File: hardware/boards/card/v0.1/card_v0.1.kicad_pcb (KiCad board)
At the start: 6 copper layers, 67.6 x 25.4 mm, 19 parts, among them IC1 IS42S16160J-7BLI, IC2 IS42S16160J-7BLI, J1 SODIMM-200, U2 STM32H747XIHx

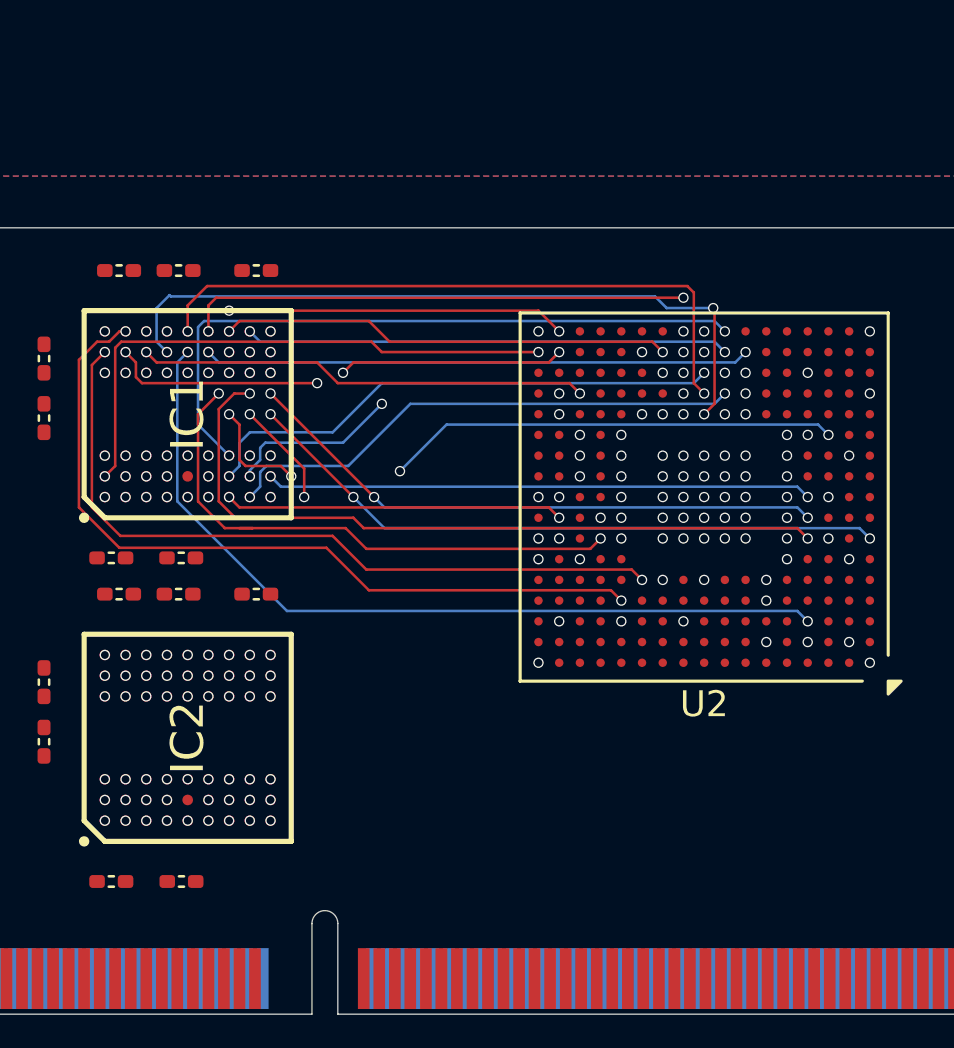
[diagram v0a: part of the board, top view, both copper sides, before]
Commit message: boards/card: begin routing USB differential pairs
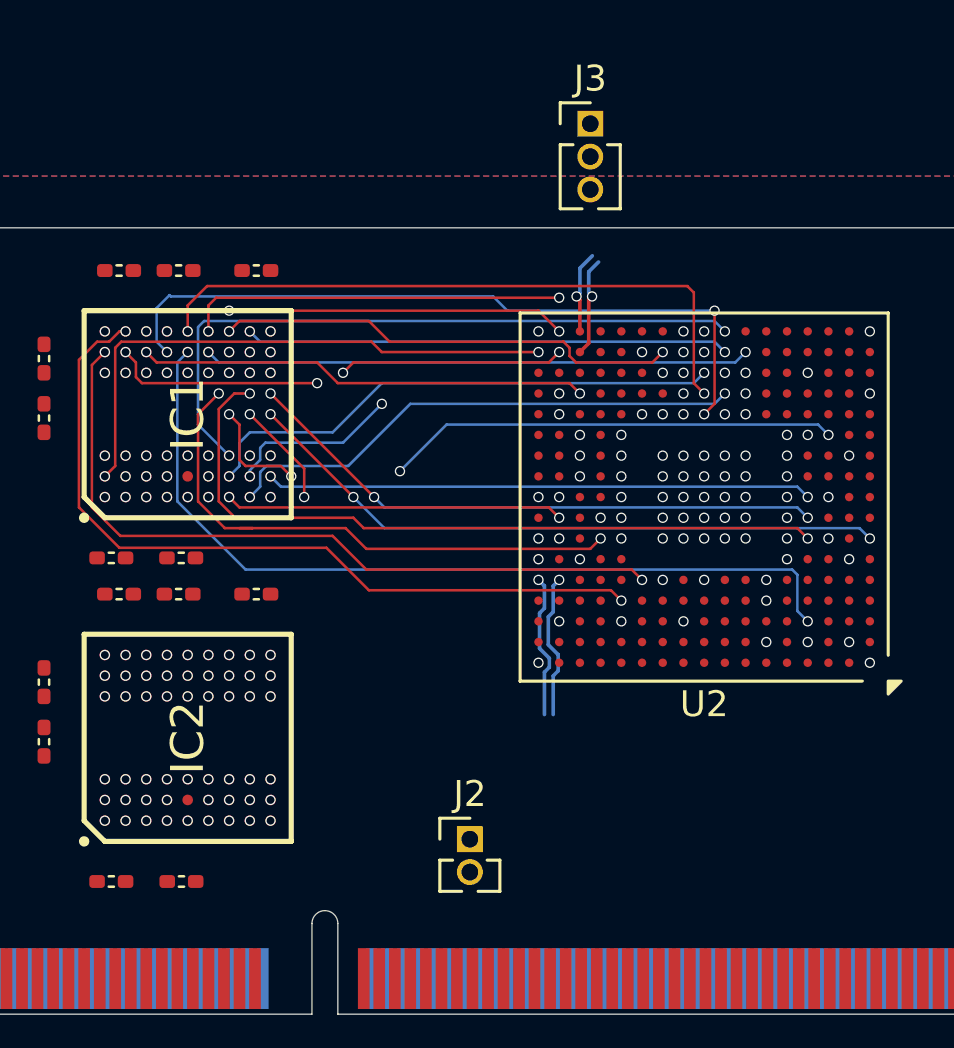
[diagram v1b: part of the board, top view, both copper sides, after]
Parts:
- added J2: USB_HOST, Connector_PinHeader_1.27mm:PinHeader_1x02_P1.27mm_Vertical, F.Cu at (71.7, 69.6)
- added J3: USB_DEVICE, Connector_PinHeader_1.27mm:PinHeader_1x03_P1.27mm_Vertical, F.Cu at (76.3, 42.0)
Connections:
- C10 pad 1: Net-(C10-Pad1) -> +3.3V
- C11 pad 1: Net-(C11-Pad1) -> +3.3V
- C12 pad 1: Net-(C11-Pad1) -> +3.3V
- C13 pad 1: Net-(C11-Pad1) -> +3.3V
- C14 pad 1: Net-(C11-Pad1) -> +3.3V
- C8 pad 1: Net-(C10-Pad1) -> +3.3V
- C9 pad 1: Net-(C10-Pad1) -> +3.3V
- IC2 pad A7: Net-(C11-Pad1) -> +3.3V
- IC2 pad A9: Net-(C10-Pad1) -> +3.3V
- IC2 pad B3: Net-(C11-Pad1) -> +3.3V
- IC2 pad C7: Net-(C11-Pad1) -> +3.3V
- IC2 pad D3: Net-(C11-Pad1) -> +3.3V
- IC2 pad E7: Net-(C10-Pad1) -> +3.3V
- IC2 pad J9: Net-(C10-Pad1) -> +3.3V
- U2 pad E16: unconnected-(U2-PA12-PadE16) -> /USB_OTG_FS_D+
- U2 pad E17: unconnected-(U2-PA11-PadE17) -> /USB_OTG_FS_D-
- U2 pad T15: unconnected-(U2-PB15-PadT15) -> /USB_OTG_HS_D+
- U2 pad U14: unconnected-(U2-PB13-PadU14) -> /USB_OTG_HS_VBUS
- U2 pad U15: unconnected-(U2-PB14-PadU15) -> /USB_OTG_HS_D-
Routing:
- net /USB_OTG_FS_D+: track 0.00 -> 5.61 mm, vias 0 -> 1
- net /USB_OTG_FS_D-: track 0.00 -> 5.61 mm, vias 0 -> 1
- net /USB_OTG_HS_D+: track 0.00 -> 3.89 mm, vias 0 -> 1
- net /USB_OTG_HS_D-: track 0.00 -> 3.23 mm, vias 0 -> 1
- net /FMC_NBL0: track 32.2 -> 33.0 mm
- net /FMC_SDNE1: track 17.4 -> 17.9 mm
- net Net-(C11-Pad1): vias 4 -> 0
- net Net-(C10-Pad1): vias 3 -> 0
- net +3.3V: vias 29 -> 36
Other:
- board text added: "Stackup: JLC06101H-3313 1mm thickness (inner 0.5Oz, outter 1Oz) USB: 90Ω Coplanar Differential Pair: 0.14mm width, 0.2mm spacing"

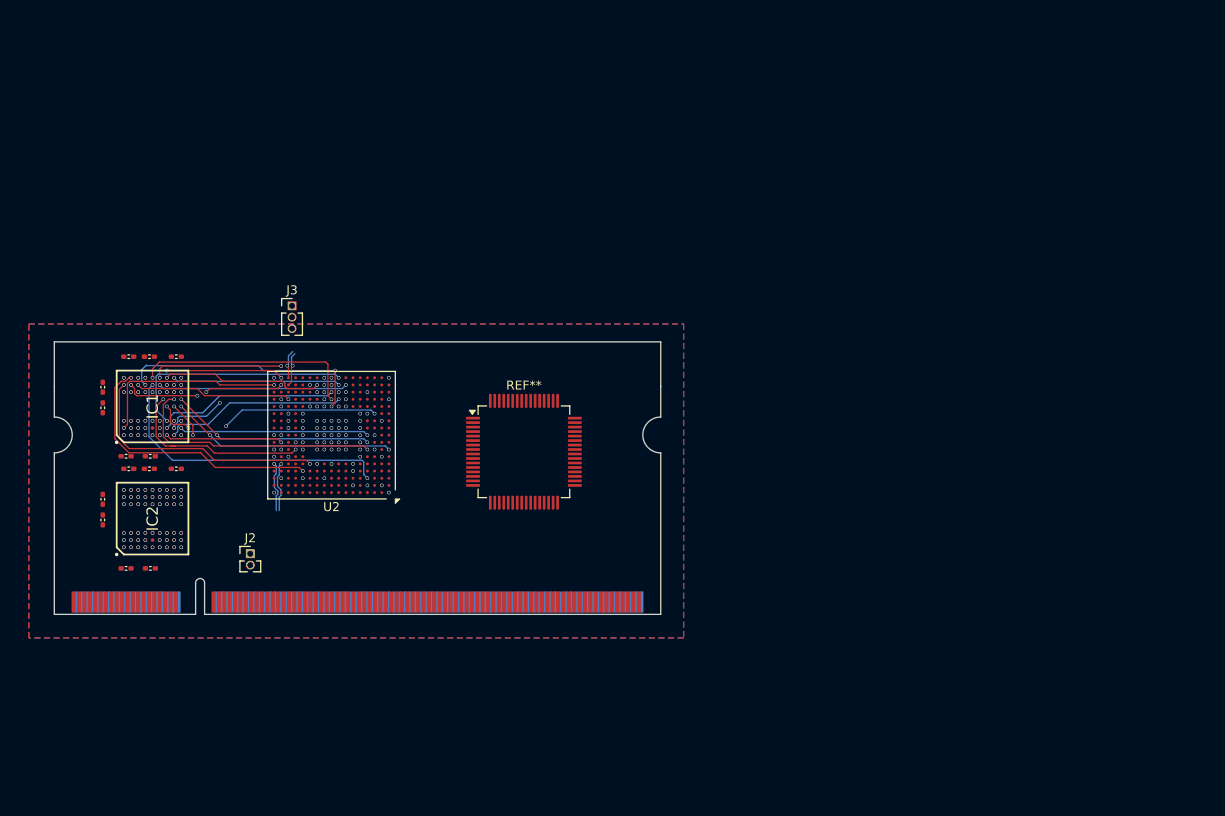
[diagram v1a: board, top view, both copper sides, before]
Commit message: boards/card: routing of essential components and audio codec
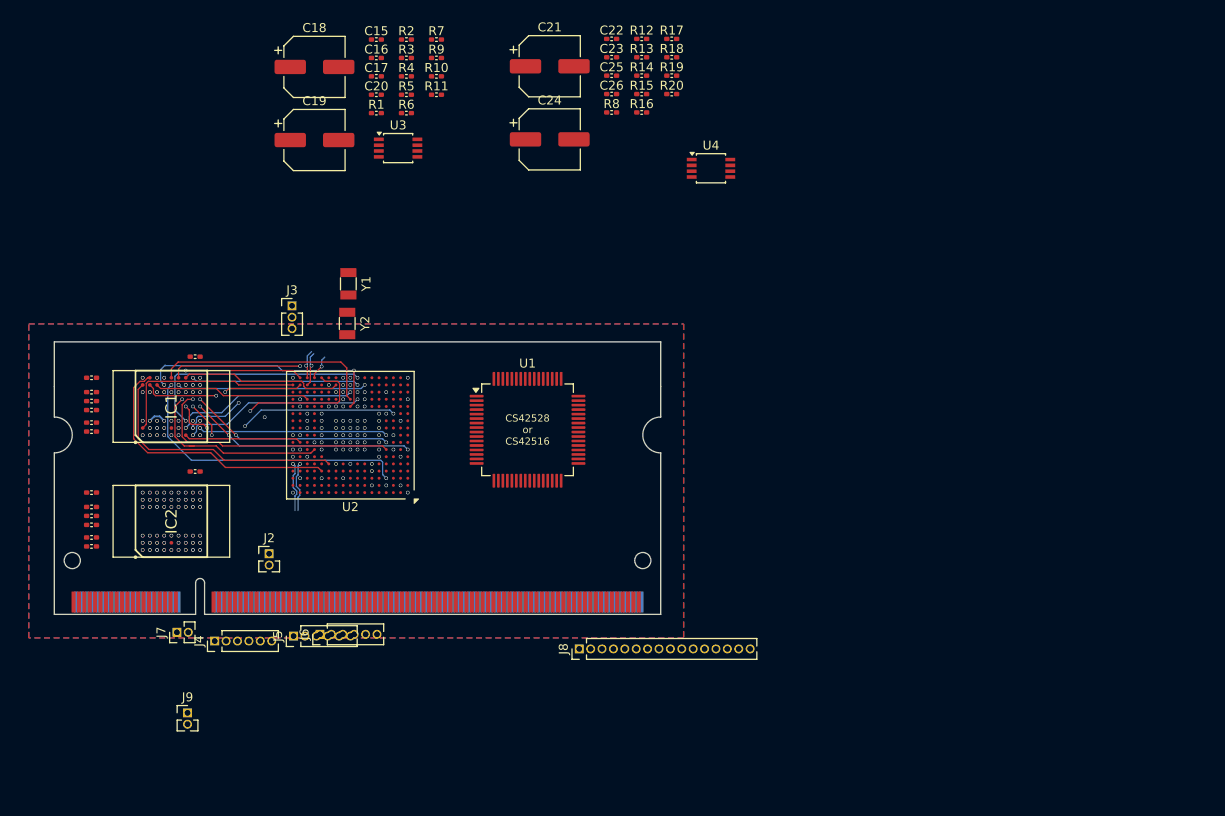
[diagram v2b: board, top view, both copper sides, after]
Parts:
- removed REF**: LQFP-64_10x10mm_P0.5mm, Package_QFP:LQFP-64_10x10mm_P0.5mm
- added C15: 2700pF C0G, rhais_rcl.pretty-main:C0402, F.Cu at (85.8, 12.3)
- added C16: 470pF C0G, rhais_rcl.pretty-main:C0402, F.Cu at (85.8, 14.3)
- added C17: 470pF C0G, rhais_rcl.pretty-main:C0402, F.Cu at (85.8, 16.4)
- added C18: 100uF ELEC, Capacitor_SMD:CP_Elec_6.3x5.7, F.Cu at (78.8, 15.3)
- added C19: 100uF ELEC, Capacitor_SMD:CP_Elec_6.3x5.7, F.Cu at (78.8, 23.5)
- added C20: 0.1uF X7R, rhais_rcl.pretty-main:C0402, F.Cu at (85.8, 18.4)
- added C21: 100uF ELEC, Capacitor_SMD:CP_Elec_6.3x5.7, F.Cu at (105.1, 15.3)
- added C22: 0.1uF X7R, rhais_rcl.pretty-main:C0402, F.Cu at (112.0, 12.2)
- added C23: 470pF C0G, rhais_rcl.pretty-main:C0402, F.Cu at (112.0, 14.3)
- added C24: 100uF ELEC, Capacitor_SMD:CP_Elec_6.3x5.7, F.Cu at (105.1, 23.4)
- added C25: 470pF C0G, rhais_rcl.pretty-main:C0402, F.Cu at (112.0, 16.3)
- added C26: 2700pF C0G, rhais_rcl.pretty-main:C0402, F.Cu at (112.0, 18.4)
- added J4: SD_CARD, Connector_PinHeader_1.27mm:PinHeader_1x06_P1.27mm_Vertical, F.Cu at (67.7, 79.3)
- added J5: DEBUG, Connector_PinHeader_1.27mm:PinHeader_1x06_P1.27mm_Vertical, F.Cu at (76.5, 78.8)
- added J6: SPI, Connector_PinHeader_1.27mm:PinHeader_1x06_P1.27mm_Vertical, F.Cu at (79.5, 78.6)
- added J7: UART4, Connector_PinHeader_1.27mm:PinHeader_1x02_P1.27mm_Vertical, F.Cu at (63.5, 78.4)
- added J8: Conn_01x16_Pin, Connector_PinHeader_1.27mm:PinHeader_1x16_P1.27mm_Vertical, F.Cu at (108.4, 80.2)
- added J9: AUDIO_IN, Connector_PinHeader_1.27mm:PinHeader_1x02_P1.27mm_Vertical, F.Cu at (64.7, 87.3)
- added R1: 91R, rhais_rcl.pretty-main:R0402, F.Cu at (85.8, 20.5)
- added R10: 3.32k, rhais_rcl.pretty-main:R0402, F.Cu at (92.5, 16.4)
- added R11: 100k, rhais_rcl.pretty-main:R0402, F.Cu at (92.5, 18.4)
- added R12: 100k, rhais_rcl.pretty-main:R0402, F.Cu at (115.3, 12.2)
- added R13: 2.8k, rhais_rcl.pretty-main:R0402, F.Cu at (115.3, 14.3)
- added R14: 3.32k, rhais_rcl.pretty-main:R0402, F.Cu at (115.3, 16.3)
- added R15: 634R, rhais_rcl.pretty-main:R0402, F.Cu at (115.3, 18.4)
- added R16: 332R, rhais_rcl.pretty-main:R0402, F.Cu at (115.3, 20.4)
- added R17: 634R, rhais_rcl.pretty-main:R0402, F.Cu at (118.7, 12.2)
- added R18: 91R, rhais_rcl.pretty-main:R0402, F.Cu at (118.7, 14.3)
- added R19: 634R, rhais_rcl.pretty-main:R0402, F.Cu at (118.7, 16.3)
- added R2: 634R, rhais_rcl.pretty-main:R0402, F.Cu at (89.1, 12.3)
- added R20: 91R, rhais_rcl.pretty-main:R0402, F.Cu at (118.7, 18.4)
- added R3: 634R, rhais_rcl.pretty-main:R0402, F.Cu at (89.1, 14.3)
- added R4: 91R, rhais_rcl.pretty-main:R0402, F.Cu at (89.1, 16.4)
- added R5: 634R, rhais_rcl.pretty-main:R0402, F.Cu at (89.1, 18.4)
- added R6: 332R, rhais_rcl.pretty-main:R0402, F.Cu at (89.1, 20.5)
- added R7: 10k, rhais_rcl.pretty-main:R0402, F.Cu at (92.5, 12.3)
- added R8: 10k, rhais_rcl.pretty-main:R0402, F.Cu at (112.0, 20.4)
- added R9: 2.8k, rhais_rcl.pretty-main:R0402, F.Cu at (92.5, 14.3)
- added U1: CS42528K-CQZ, Package_QFP:LQFP-64_10x10mm_P0.5mm, F.Cu at (102.6, 55.8)
- added U3: NJM4580E-TE1, Package_SO:TSSOP-8_3x3mm_P0.65mm, F.Cu at (88.2, 24.4)
- added U4: NJM4580E-TE1, Package_SO:TSSOP-8_3x3mm_P0.65mm, F.Cu at (123.0, 26.6)
- added Y1: Crystal, Crystal:Crystal_SMD_3215-2Pin_3.2x1.5mm, F.Cu at (82.6, 39.5)
- added Y2: Crystal, Crystal:Crystal_SMD_3215-2Pin_3.2x1.5mm, F.Cu at (82.5, 44.0)
- moved C9 8.98 mm to (54.0, 66.4)
- moved C2 7.56 mm to (54.0, 51.6)
- moved C6 7.10 mm to (54.0, 56.0), turned to 180 degrees
- moved C13 7.00 mm to (54.0, 68.8), turned to 180 degrees
- moved C5 5.37 mm to (54.0, 55.0)
- moved C14 5.17 mm to (54.0, 67.8)
- moved C10 4.92 mm to (54.0, 62.8), turned to 180 degrees
- moved C1 4.77 mm to (54.0, 50.0), turned to 180 degrees
- moved IC2 2.12 mm to (62.9, 66.0)
- moved C8 2.12 mm to (65.5, 60.5)
- moved IC1 2.10 mm to (62.9, 53.2)
- moved C3 2.10 mm to (65.5, 47.6)
- moved J2 2.10 mm to (73.8, 69.6)
- moved U2 2.10 mm to (82.8, 56.4)
- moved C4 1.99 mm to (54.0, 52.6), turned to 180 degrees
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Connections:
- IC1 pad F3: /FMC_SDCKE0 -> /FMC_SDCKE1
- IC2 pad F3: unconnected-(IC2-CKE-PadF3) -> /FMC_SDCKE0
- U2 pad A10: unconnected-(U2-PG9-PadA10) -> /SPI1_MISO
- U2 pad A13: unconnected-(U2-PC10-PadA13) -> /SDMMC1_D2
- U2 pad A2: unconnected-(U2-PI6-PadA2) -> /SAI2_SD_A
- U2 pad A9: unconnected-(U2-PG10-PadA9) -> /SPI1_NSS
- U2 pad B13: unconnected-(U2-PC11-PadB13) -> /SDMMC1_D3
- U2 pad B17: unconnected-(U2-PH14-PadB17) -> /UART4_RX
- U2 pad B9: unconnected-(U2-PG11-PadB9) -> /SPI1_SCK
- U2 pad C1: unconnected-(U2-PC15-PadC1) -> Net-(U2-PC15)
- U2 pad C11: unconnected-(U2-PD7-PadC11) -> /SPI1_MOSI
- U2 pad C12: unconnected-(U2-PC12-PadC12) -> /SDMMC1_CK
- U2 pad C2: unconnected-(U2-PC14-PadC2) -> Net-(U2-PC14)
- U2 pad C3: unconnected-(U2-PE2-PadC3) -> /SAI1_MCLK_A
- U2 pad D1: unconnected-(U2-PE5-PadD1) -> /SAI1_SCK_A
- U2 pad D12: unconnected-(U2-PD2-PadD12) -> /SDMMC1_CMD
- U2 pad D16: unconnected-(U2-PH13-PadD16) -> /UART4_TX
- U2 pad D2: unconnected-(U2-PE4-PadD2) -> /SAI1_FS_A
- U2 pad D3: unconnected-(U2-PE3-PadD3) -> /SAI1_SD_B
- U2 pad E13: unconnected-(U2-PC8-PadE13) -> /SDMMC1_D0
- U2 pad E14: unconnected-(U2-PC9-PadE14) -> /SDMMC1_D1
- U2 pad E5: unconnected-(U2-PE6-PadE5) -> /SAI1_SD_A
- U2 pad J1: unconnected-(U2-PH1-PadJ1) -> Net-(U2-PH1)
- U2 pad J2: unconnected-(U2-PH0-PadJ2) -> Net-(U2-PH0)
- U2 pad K2: unconnected-(U2-PF6-PadK2) -> /SAI4_SD_B
- U2 pad N5: unconnected-(U2-PA0-PadN5) -> /SAI2_SD_B
- U2 pad P3: unconnected-(U2-PH4-PadP3) -> /I2C2_SCL
- U2 pad P4: unconnected-(U2-PH5-PadP4) -> /I2C2_SDA
- U2 pad U13: unconnected-(U2-PH7-PadU13) -> /FMC_SDCKE1
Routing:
- net /FMC_SDCKE1: track 0.00 -> 23.1 mm, vias 0 -> 2
- net /USB_OTG_HS_VBUS: track 0.00 -> 2.78 mm, vias 0 -> 1
- net +3.3V: track 0.00 -> 2.01 mm
- net /FMC_D6: track 25.0 -> 24.8 mm, vias 2 -> 0
- net /FMC_SDCKE0: vias 2 -> 3
- net /FMC_SDNE1: vias 2 -> 0
- net /FMC_A12: vias 2 -> 0
- net /FMC_D7: vias 3 -> 2
- net /FMC_D0: vias 3 -> 2
- net /FMC_BA1: vias 3 -> 2
- net /FMC_D15: vias 3 -> 2
- net /FMC_D14: vias 2 -> 0
- net /FMC_D1: vias 2 -> 0
- net /FMC_A0: vias 3 -> 2
- net unconnected-(IC2-CKE-PadF3): vias 1 -> 0
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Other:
- board text added: "CS42528 or CS42516"
- board text added: "Stackup: JLC06101H-3313 1mm thickness (inner 0.5 Oz, outter 1 Oz) USB: 90Ω Coplanar Differential Pair: 0.14mm width, 0.2mm spacing"
- board text added: "TODO: may need to change codec due to ELECs"
- board text removed: "Stackup: JLC06101H-3313 1mm thickness (inner 0.5Oz, outter 1Oz) USB: 90Ω Coplanar Differential Pair: 0.14mm width, 0.2mm spacing"
